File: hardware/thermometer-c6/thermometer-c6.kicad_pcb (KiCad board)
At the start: 2 copper layers, 48 x 35 mm, 101 parts, among them J1 JST-PH-2 BAT, J2 MEAS_HDR, J3 USB-C, J4 EPD FPC24 0.5mm, J5 DEBUG, Q1 AO3401A, Q2 AO3401A, Q3 Si1308EDL, Q4 AO3401A, Q5 2N7002, Q6 AO3401A, SW1 RESET, SW2 BOOT, U1 ESP32-C6-MINI-1-N4, U2 RT9080-33GJ5, U3 USBLC6-2SC6, U4 MCP73831-2, U5 BMP581, U6 BMP585, Y1 32.768kHz FC-135

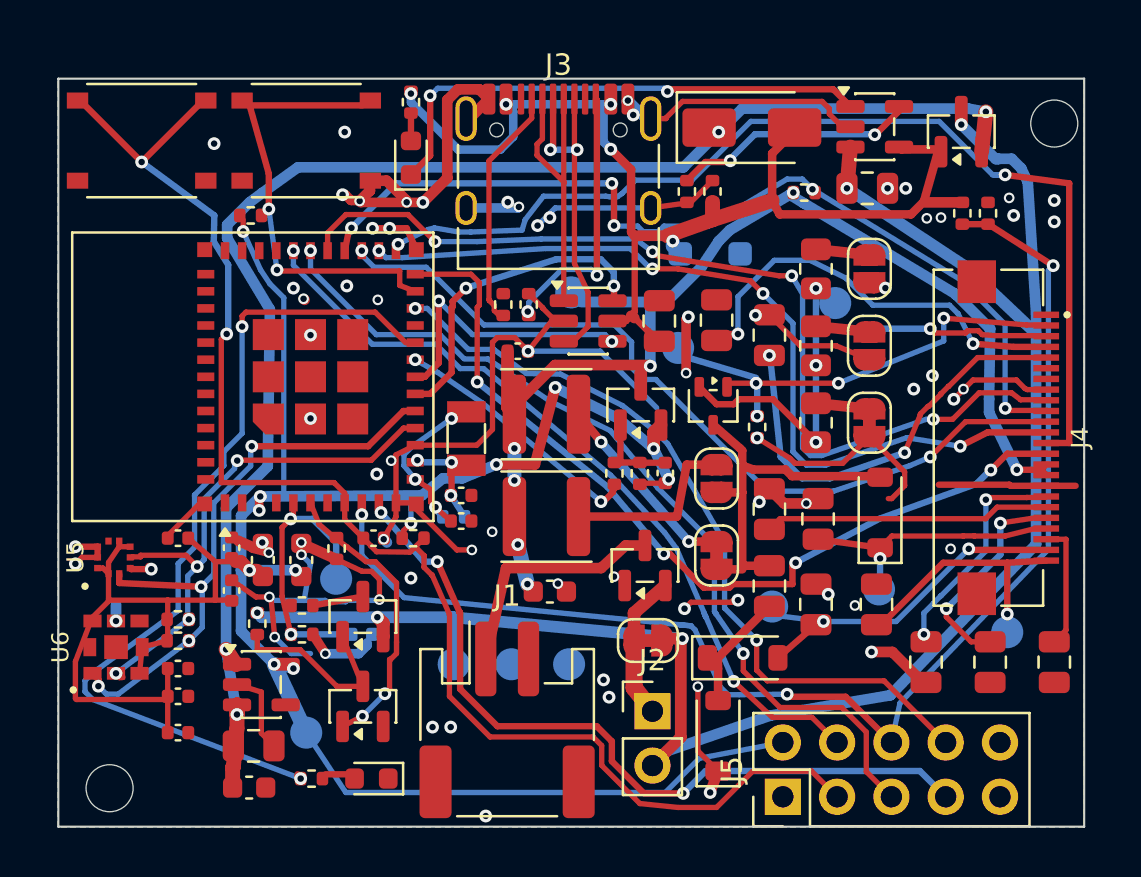
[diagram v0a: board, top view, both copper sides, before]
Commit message: M7: author functional silkscreen labels (test points, jumpers, J5, safety)
31 SILK entries: 11 mirrored bottom-side test-point labels (VBAT/GND/3V3/EPD_VCC/PREVGH/PREVGL/GDR/RESE/VCOM/VBAT_ADC), jumper values in standard units with bridge-ONE hints (RESE 0.47Ohm*/2.2/3, 10uH*/47uH), J5 pin legend, RST/BOOT/CHG/STAT, BAT + polarity, PPK2, fit ONE, CHARGE INDOORS 0-45C, board rev. Adds REF_POS (reposition kept refs J2/J4/J5/U6) + SILK_TO_FAB (move J5/JP5/JP6/U1-poly silk graphics to fab) mechanisms; relaxes silk min text height 0.8->0.4 and pins lib_footprint_mismatch=ignore (intentional F.Fab divergence). DRC 0 silk violations (overlap/edge/over-copper all 0), check_pcb required strings present, make check green, copper gate REAL=0, byte-stable, glyphs Omega/mu/deg render, bottom labels mirror-correct.

Co-Authored-By: Claude Opus 4.8 (1M context) <noreply@anthropic.com>
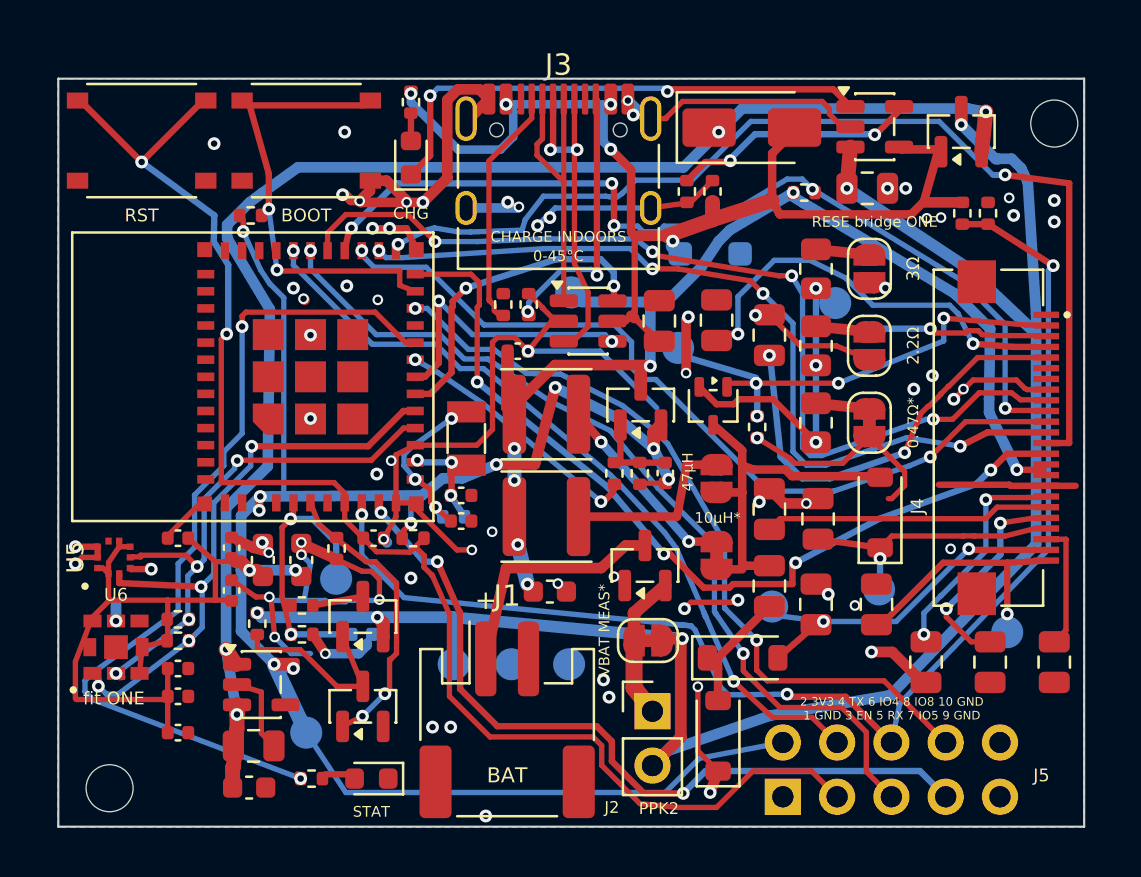
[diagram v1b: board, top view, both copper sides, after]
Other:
- board text added: "+"
- board text added: "0-45°C"
- board text added: "0.47Ω*"
- board text added: "10µH*"
- board text added: "2 3V3 4 TX 6 IO4 8 IO8 10 GND 1 GND 3 EN 5 RX 7 IO5 9 GND"
- board text added: "2.2Ω"
- board text added: "3V3"
- board text added: "3Ω"
- board text added: "47µH"
- board text added: "BAT"
- board text added: "BOOT"
- board text added: "CHARGE INDOORS"
- board text added: "CHG"
- board text added: "EPD_VCC"
- board text added: "GDR"
- board text added: "GND"
- board text added: "IND bridge ONE"
- board text added: "PPK2"
- board text added: "PREVGH"
- board text added: "PREVGL"
- board text added: "RESE"
- board text added: "RESE bridge ONE"
- board text added: "RST"
- board text added: "STAT"
- board text added: "VBAT"
- board text added: "VBAT MEAS*"
- board text added: "VBAT_ADC"
- board text added: "VCOM"
- board text added: "fit ONE"
- board text added: "thermometer-c6 rev A"

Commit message: M7: resize silk to legibility-first (>=0.8mm/0.15mm); consolidate hints; drop non-fitting labels
Every authored silk label now >=0.8mm height / 0.15mm line (min_text_height/thickness floors in .kicad_pro + add_silk thickness floor). 28 labels: TOP position-specific beside their part (RST/BOOT/CHG/STAT, BAT + polarity, PPK2, RESE 0.47/2.2/3Ohm values, 10uH, DBG marker); BACK mirrored (11 test-point labels + CHARGE INDOORS/0-45C/rev + a self-explanatory 'bridge ONE' legend naming both jumper groups RESE=JP2/3/4 & IND=JP5/6 + fit ONE). No '*' default markers. Occlusion 0 (CHARGE INDOORS/0-45C moved off J3's body to the back). Dropped/relocated for space at 0.8mm: J5 per-pin legend (kept DBG marker; pinout -> README), JP1 VBAT MEAS (covered by PPK2 + Fab MEAS), JP6 47uH value (into back legend); J2/J4 refdes -> F.Fab (function label wins the boxed courtyard). DRC 0 (silk + text-size), check_pcb OK, make check green, copper gate REAL=0, byte-stable.

Co-Authored-By: Claude Opus 4.8 (1M context) <noreply@anthropic.com>
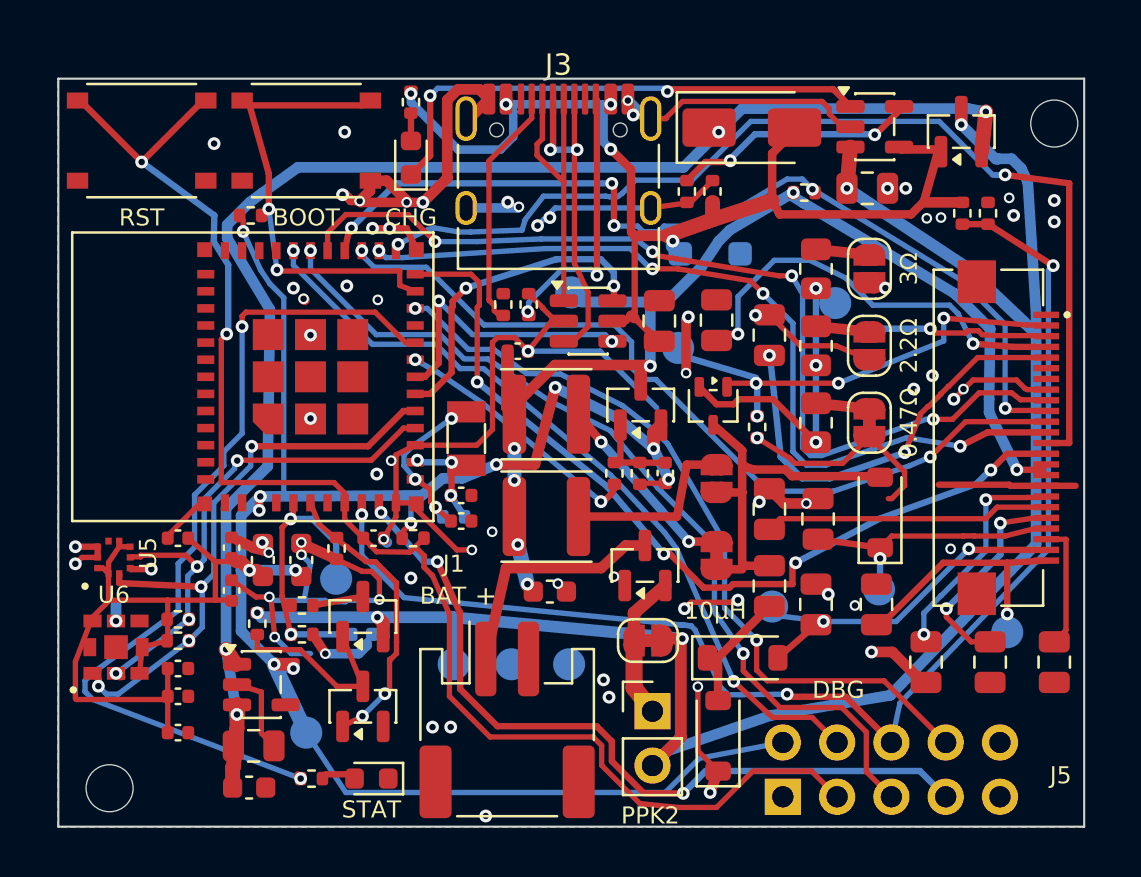
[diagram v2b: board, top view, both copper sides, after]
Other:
- board text added: "0.47Ω"
- board text added: "10µH"
- board text added: "DBG"
- board text added: "bridge ONE RESE 0.47/2.2/3Ω=JP2/3/4 IND 10/47µH=JP5/6"
- board text removed: "0.47Ω*"
- board text removed: "10µH*"
- board text removed: "2 3V3 4 TX 6 IO4 8 IO8 10 GND 1 GND 3 EN 5 RX 7 IO5 9 GND"
- board text removed: "47µH"
- board text removed: "IND bridge ONE"
- board text removed: "RESE bridge ONE"
- board text removed: "VBAT MEAS*"
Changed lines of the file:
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@@
 	)
 	(gr_text "+"
-		(at 120 124.4 0)
+		(at 120 124.2 0)
 		(layer "F.SilkS")
 		(effects
 			(font
 				(size 0.9 0.9)
-				(thickness 0.14)
+				(thickness 0.15)
 			)
 		)
 	)
 	(gr_text "0-45°C"
-		(at 123.4 108.3 0)
-		(layer "F.SilkS")
-		(effects
-			(font
-				(size 0.5 0.5)
-				(thickness 0.07)
-			)
-		)
-	)
-	(gr_text "0.47Ω*"
-		(at 140 116.1 90)
-		(layer "F.SilkS")
+		(at 120.5 116.5 0)
+		(layer "B.SilkS")
 		(effects
 			(font
-				(size 0.5 0.5)
-				(thickness 0.07)
+				(size 0.8 0.8)
+				(thickness 0.15)
 			)
+			(justify mirror)
 		)
 	)
-	(gr_text "10µH*"
-		(at 130.85 120.55 0)
+	(gr_text "0.47Ω"
+		(at 139.8 116.1 90)
 		(layer "F.SilkS")
 		(effects
 			(font
-				(size 0.5 0.5)
-				(thickness 0.07)
+				(size 0.8 0.8)
+				(thickness 0.15)
 			)
 		)
 	)
-	(gr_text "2 3V3 4 TX 6 IO4 8 IO8 10 GND\n1 GND 3 EN 5 RX 7 IO5 9 GND"
-		(at 139 129.475 0)
+	(gr_text "10µH"
+		(at 130.74 124.9 0)
 		(layer "F.SilkS")
 		(effects
 			(font
-				(size 0.4 0.4)
-				(thickness 0.06)
+				(size 0.8 0.8)
+				(thickness 0.15)
 			)
 		)
 	)
 	(gr_text "2.2Ω"
-		(at 140 112.5 90)
+		(at 139.8 112.5 90)
 		(layer "F.SilkS")
 		(effects
 			(font
-				(size 0.55 0.55)
-				(thickness 0.08)
+				(size 0.8 0.8)
+				(thickness 0.15)
 			)
 		)
@@
 		(effects
 			(font
-				(size 0.7 0.7)
-				(thickness 0.1)
+				(size 0.8 0.8)
+				(thickness 0.15)
 			)
 			(justify mirror)
@@
 	)
 	(gr_text "3Ω"
-		(at 140 108.9 90)
+		(at 139.8 108.9 90)
 		(layer "F.SilkS")
 		(effects
 			(font
-				(size 0.6 0.6)
-				(thickness 0.09)
+				(size 0.8 0.8)
+				(thickness 0.15)
 			)
 		)
 	)
-	(gr_text "47µH"
-		(at 129.449999 118.4 90)
+	(gr_text "BAT"
+		(at 118 124.2 0)
 		(layer "F.SilkS")
 		(effects
 			(font
-				(size 0.5 0.5)
-				(thickness 0.07)
+				(size 0.8 0.8)
+				(thickness 0.15)
 			)
 		)
 	)
-	(gr_text "BAT"
-		(at 121 132.6 0)
+	(gr_text "BOOT"
+		(at 111.6 106.5 0)
 		(layer "F.SilkS")
 		(effects
 			(font
-				(size 0.7 0.7)
-				(thickness 0.1)
+				(size 0.8 0.8)
+				(thickness 0.15)
 			)
 		)
 	)
-	(gr_text "BOOT"
-		(at 111.6 106.4 0)
-		(layer "F.SilkS")
+	(gr_text "CHARGE INDOORS"
+		(at 120.5 115 0)
+		(layer "B.SilkS")
 		(effects
 			(font
-				(size 0.6 0.6)
-				(thickness 0.09)
+				(size 0.8 0.8)
+				(thickness 0.15)
 			)
+			(justify mirror)
 		)
 	)
-	(gr_text "CHARGE INDOORS"
-		(at 123.4 107.4 0)
+	(gr_text "CHG"
+		(at 116.5 106.5 0)
 		(layer "F.SilkS")
 		(effects
 			(font
-				(size 0.5 0.5)
-				(thickness 0.07)
+				(size 0.8 0.8)
+				(thickness 0.15)
 			)
 		)
 	)
-	(gr_text "CHG"
-		(at 116.5 106.3 0)
+	(gr_text "DBG"
+		(at 136.5 128.6 0)
 		(layer "F.SilkS")
 		(effects
 			(font
-				(size 0.55 0.55)
-				(thickness 0.08)
+				(size 0.8 0.8)
+				(thickness 0.15)
 			)
 		)
 	)
 	(gr_text "EPD_VCC"
-		(at 124 111.8 0)
+		(at 124 111.9 0)
 		(layer "B.SilkS")
 		(effects
 			(font
-				(size 0.7 0.7)
-				(thickness 0.1)
+				(size 0.8 0.8)
+				(thickness 0.15)
 			)
 			(justify mirror)
@@
 		(effects
 			(font
-				(size 0.7 0.7)
-				(thickness 0.1)
+				(size 0.8 0.8)
+				(thickness 0.15)
 			)
 			(justify mirror)
@@
 		(effects
 			(font
-				(size 0.7 0.7)
-				(thickness 0.1)
+				(size 0.8 0.8)
+				(thickness 0.15)
 			)
 			(justify mirror)
@@
 		(effects
 			(font
-				(size 0.7 0.7)
-				(thickness 0.1)
-			)
-			(justify mirror)
-		)
-	)
-	(gr_text "IND bridge ONE"
-		(at 130.8 120.5 0)
-		(layer "B.SilkS")
-		(effects
-			(font
-				(size 0.6 0.6)
-				(thickness 0.09)
+				(size 0.8 0.8)
+				(thickness 0.15)
 			)
 			(justify mirror)
@@
 	)
 	(gr_text "PPK2"
-		(at 128.1 134.15 0)
+		(at 127.7 134.48 0)
 		(layer "F.SilkS")
 		(effects
 			(font
-				(size 0.55 0.55)
-				(thickness 0.08)
+				(size 0.8 0.8)
+				(thickness 0.15)
 			)
 		)
@@
 		(effects
 			(font
-				(size 0.7 0.7)
-				(thickness 0.1)
+				(size 0.8 0.8)
+				(thickness 0.15)
 			)
 			(justify mirror)
@@
 		(effects
 			(font
-				(size 0.7 0.7)
-				(thickness 0.1)
+				(size 0.8 0.8)
+				(thickness 0.15)
 			)
 			(justify mirror)
 		)
 	)
-	(gr_text "RESE bridge ONE"
-		(at 138.2 106.7 0)
-		(layer "F.SilkS")
-		(effects
-			(font
-				(size 0.5 0.5)
-				(thickness 0.07)
-			)
-		)
-	)
 	(gr_text "RESE"
 		(at 136.35 112.3 0)
@@
 		(effects
 			(font
-				(size 0.7 0.7)
-				(thickness 0.1)
+				(size 0.8 0.8)
+				(thickness 0.15)
 			)
 			(justify mirror)
@@
 	)
 	(gr_text "RST"
-		(at 103.9 106.4 0)
+		(at 103.9 106.5 0)
 		(layer "F.SilkS")
 		(effects
 			(font
-				(size 0.6 0.6)
-				(thickness 0.09)
+				(size 0.8 0.8)
+				(thickness 0.15)
 			)
 		)
 	)
 	(gr_text "STAT"
-		(at 114.65 134.3 0)
+		(at 114.65 134.199999 0)
 		(layer "F.SilkS")
 		(effects
 			(font
-				(size 0.5 0.5)
-				(thickness 0.07)
-			)
-		)
-	)
-	(gr_text "VBAT MEAS*"
-		(at 125.55 125.8 90)
-		(layer "F.SilkS")
-		(effects
-			(font
-				(size 0.5 0.5)
-				(thickness 0.07)
+				(size 0.8 0.8)
+				(thickness 0.15)
 			)
 		)
@@
 		(effects
 			(font
-				(size 0.7 0.7)
-				(thickness 0.1)
+				(size 0.8 0.8)
+				(thickness 0.15)
 			)
 			(justify mirror)
@@
 		(effects
 			(font
-				(size 0.6 0.6)
-				(thickness 0.09)
+				(size 0.8 0.8)
+				(thickness 0.15)
 			)
 			(justify mirror)
@@
 		(effects
 			(font
-				(size 0.7 0.7)
-				(thickness 0.1)
+				(size 0.8 0.8)
+				(thickness 0.15)
+			)
+			(justify mirror)
+		)
+	)
+	(gr_text "bridge ONE   RESE 0.47/2.2/3Ω=JP2/3/4   IND 10/47µH=JP5/6"
+		(at 122 118.5 0)
+		(layer "B.SilkS")
+		(effects
+			(font
+				(size 0.8 0.8)
+				(thickness 0.15)
 			)
 			(justify mirror)
@@
 	)
 	(gr_text "fit ONE"
-		(at 102.6 129 0)
-		(layer "F.SilkS")
+		(at 102.6 124.3 0)
+		(layer "B.SilkS")
 		(effects
 			(font
-				(size 0.6 0.6)
-				(thickness 0.09)
+				(size 0.8 0.8)
+				(thickness 0.15)
 			)
+			(justify mirror)
 		)
 	)
 	(gr_text "thermometer-c6 rev A"
-		(at 120 116.5 0)
+		(at 120 113.3 0)
 		(layer "B.SilkS")
 		(effects
 			(font
-				(size 0.7 0.7)
-				(thickness 0.1)
+				(size 0.8 0.8)
+				(thickness 0.15)
 			)
 			(justify mirror)
@@
 		(tags "connector JST PH horizontal")
 		(property "Reference" "J1"
-			(at 0 -5.8 0)
+			(at -2.5 -7.3 0)
 			(layer "F.SilkS")
 			(effects
 				(font
-					(size 1 1)
+					(size 0.8 0.8)
 					(thickness 0.15)
 				)
@@
 		(tags "Through hole pin header THT 1x02 2.54mm single row")
 		(property "Reference" "J2"
-			(at -1.9 4.5 0)
-			(layer "F.SilkS")
+			(at 0 -2.38 0)
+			(layer "F.Fab")
 			(effects
 				(font
-					(size 0.55 0.55)
-					(thickness 0.08)
+					(size 1 1)
+					(thickness 0.15)
 				)
 			)
@@
 		(tags "Through hole pin header THT 2x05 2.54mm double row")
 		(property "Reference" "J5"
-			(at 1 12.1 0)
+			(at 1 13 0)
 			(layer "F.SilkS")
 			(effects
 				(font
-					(size 0.6 0.6)
-					(thickness 0.09)
+					(size 0.8 0.8)
+					(thickness 0.15)
 				)
 			)
@@
 		(tags "LGA BMP581 Bosch")
 		(property "Reference" "U5"
-			(at 0 -1.8 90)
+			(at 0.2 1.6 90)
 			(layer "F.SilkS")
 			(effects
 				(font
 					(size 0.8 0.8)
-					(thickness 0.12)
+					(thickness 0.15)
 				)
 			)
@@
 		(tags "LGA BMP585 Bosch")
 		(property "Reference" "U6"
-			(at 2.45 0 0)
+			(at 2.45 -0.1 0)
 			(layer "F.SilkS")
 			(effects
 				(font
-					(size 0.6 0.6)
-					(thickness 0.09)
+					(size 0.8 0.8)
+					(thickness 0.15)
 				)
 			)
@@
 		(tags "FPC FFC XUNPU 24 0.5mm dual-contact")
 		(property "Reference" "J4"
-			(at 3.2 4.4 90)
-			(layer "F.SilkS")
+			(at 0 -3.2 270)
+			(layer "F.Fab")
 			(effects
 				(font
-					(size 0.6 0.6)
-					(thickness 0.09)
+					(size 0.8 0.8)
+					(thickness 0.12)
 				)
 			)

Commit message: M7: add J5 debug-header pinout legend on back silk (mirror-correct, MOUNT TOP)
11 B.SilkS entries north of J5, column-aligned to the through-pins so the pinout reads logically from the back (upper row even/N pins +3V3/TX/IO4/IO8, lower row odd/S pins GND/EN/RX/IO5, single GND for pins 9&10). Includes a MOUNT TOP cue so the header isn't soldered to the wrong side (which would invert the pinout). All >=0.8mm/0.15mm; DRC 0 silk (incl text-size), 0 occlusion, check_pcb OK, make check green, byte-stable.

Co-Authored-By: Claude Opus 4.8 (1M context) <noreply@anthropic.com>
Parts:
- removed the H2 at (102.4, 133.2)
- added Q4: AO3401A, Package_TO_SOT_SMD:SOT-23, F.Cu at (114.2, 125.2)
- H1: renamed from Q4; value AO3401A -> M2; footprint Package_TO_SOT_SMD:SOT-23 -> MountingHole:MountingHole_2.2mm_M2
- moved H2 54.0 mm to (102.4, 133.2)
- moved H1 39.7 mm to (146.6, 102.1), turned to 0 degrees
- renumbered H1 to H2
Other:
- board text added: "+3V3"
- board text added: "EN"
- board text added: "IO4"
- board text added: "IO5"
- board text added: "IO8"
- board text added: "J5"
- board text added: "MOUNT TOP"
- board text added: "RX"
- board text added: "TX"
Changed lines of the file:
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@@
+		)
+	)
+	(gr_text "+3V3"
+		(at 133.9 128.449999 0)
+		(layer "B.SilkS")
+		(effects
+			(font
+				(size 0.8 0.8)
+				(thickness 0.15)
+			)
+			(justify mirror)
 		)
 	)
@@
 		)
 	)
+	(gr_text "EN"
+		(at 136.44 129.55 0)
+		(layer "B.SilkS")
+		(effects
+			(font
+				(size 0.8 0.8)
+				(thickness 0.15)
+			)
+			(justify mirror)
+		)
+	)
 	(gr_text "EPD_VCC"
 		(at 124 111.9 0)
@@
 		)
 	)
+	(gr_text "GND"
+		(at 133.9 129.55 0)
+		(layer "B.SilkS")
+		(effects
+			(font
+				(size 0.8 0.8)
+				(thickness 0.15)
+			)
+			(justify mirror)
+		)
+	)
+	(gr_text "GND"
+		(at 144.06 129.05 0)
+		(layer "B.SilkS")
+		(effects
+			(font
+				(size 0.8 0.8)
+				(thickness 0.15)
+			)
+			(justify mirror)
+		)
+	)
+	(gr_text "IO4"
+		(at 138.98 128.449999 0)
+		(layer "B.SilkS")
+		(effects
+			(font
+				(size 0.8 0.8)
+				(thickness 0.15)
+			)
+			(justify mirror)
+		)
+	)
+	(gr_text "IO5"
+		(at 141.52 129.55 0)
+		(layer "B.SilkS")
+		(effects
+			(font
+				(size 0.8 0.8)
+				(thickness 0.15)
+			)
+			(justify mirror)
+		)
+	)
+	(gr_text "IO8"
+		(at 141.52 128.449999 0)
+		(layer "B.SilkS")
+		(effects
+			(font
+				(size 0.8 0.8)
+				(thickness 0.15)
+			)
+			(justify mirror)
+		)
+	)
+	(gr_text "J5"
+		(at 131.199999 128.949999 0)
+		(layer "B.SilkS")
+		(effects
+			(font
+				(size 0.8 0.8)
+				(thickness 0.15)
+			)
+			(justify mirror)
+		)
+	)
+	(gr_text "MOUNT TOP"
+		(at 139 127.35 0)
+		(layer "B.SilkS")
+		(effects
+			(font
+				(size 0.8 0.8)
+				(thickness 0.15)
+			)
+			(justify mirror)
+		)
+	)
 	(gr_text "PPK2"
 		(at 127.7 134.48 0)
@@
 		)
 	)
+	(gr_text "RX"
+		(at 138.98 129.55 0)
+		(layer "B.SilkS")
+		(effects
+			(font
+				(size 0.8 0.8)
+				(thickness 0.15)
+			)
+			(justify mirror)
+		)
+	)
 	(gr_text "STAT"
 		(at 114.65 134.199999 0)
@@
 		)
 	)
+	(gr_text "TX"
+		(at 136.44 128.449999 0)
+		(layer "B.SilkS")
+		(effects
+			(font
+				(size 0.8 0.8)
+				(thickness 0.15)
+			)
+			(justify mirror)
+		)
+	)
